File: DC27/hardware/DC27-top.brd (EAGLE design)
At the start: 102.4 x 117.6 mm, 32 parts

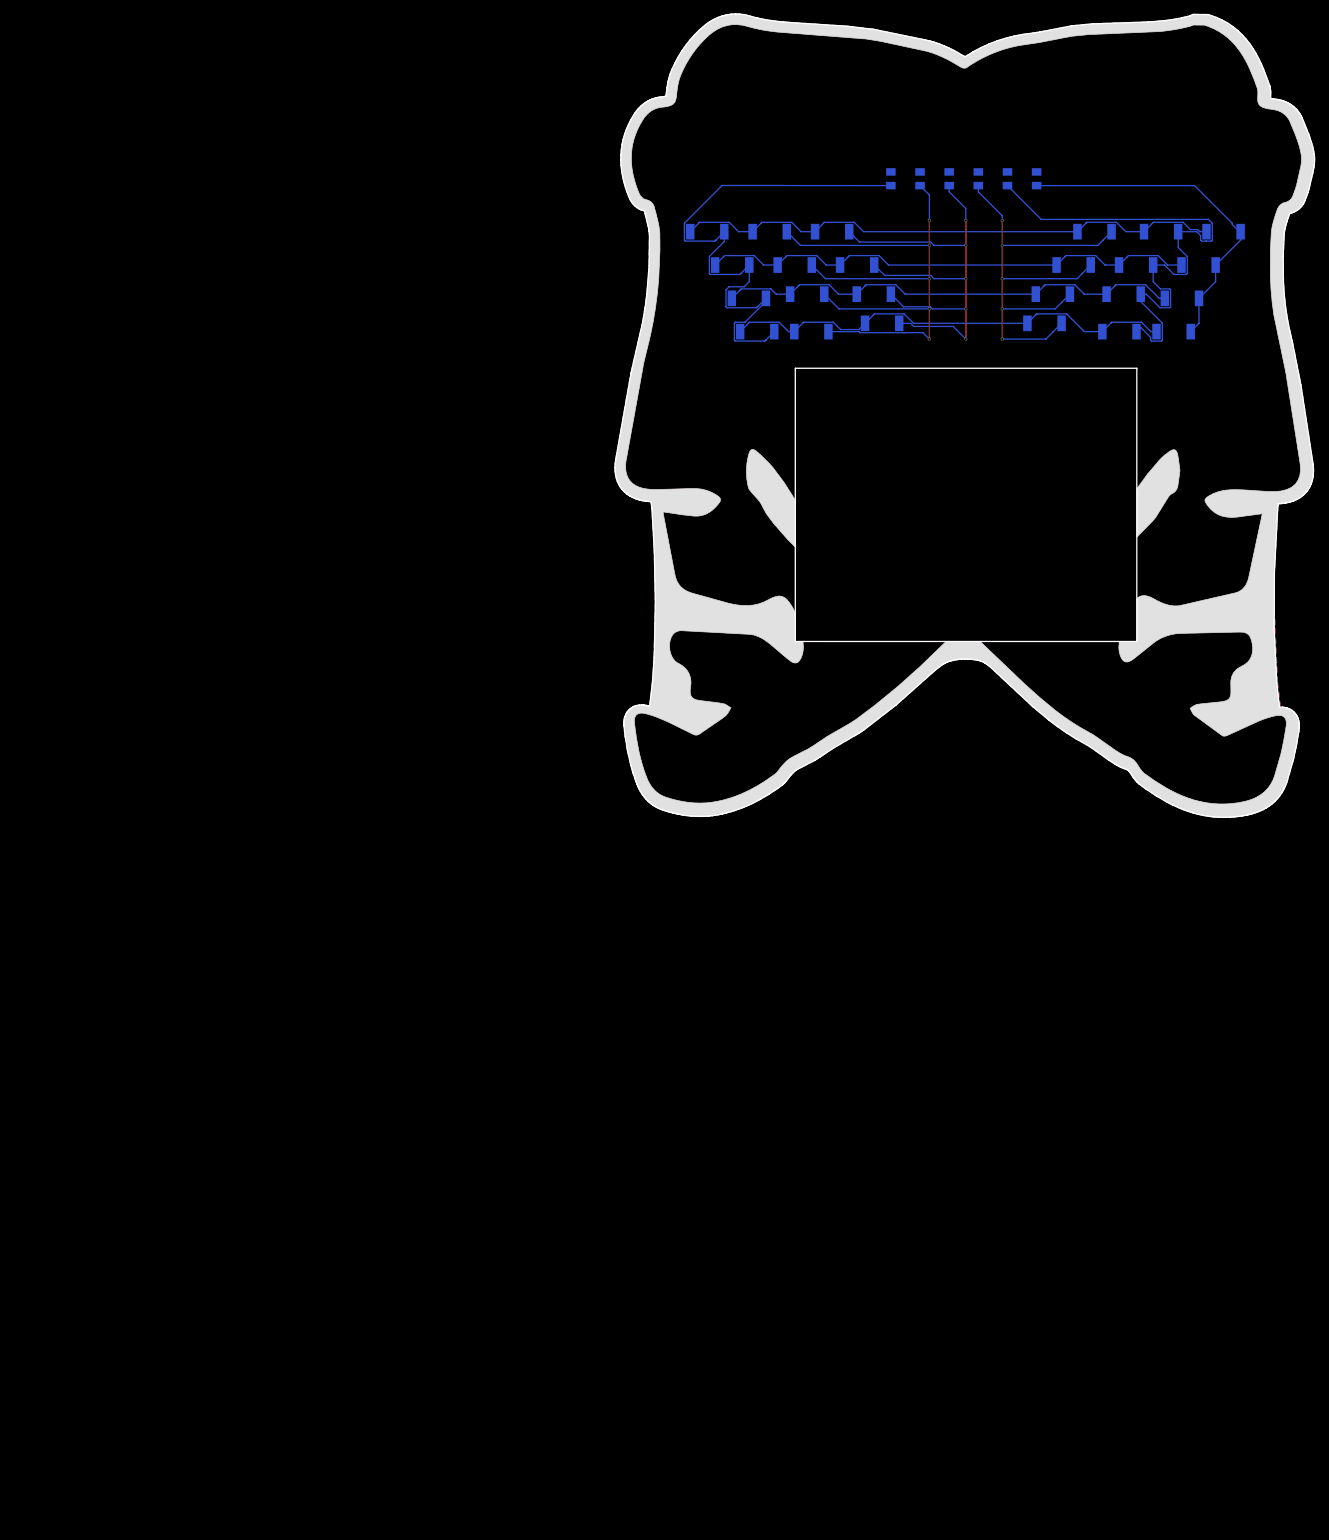
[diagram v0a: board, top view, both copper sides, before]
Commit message: adding basic layout dc27 badge
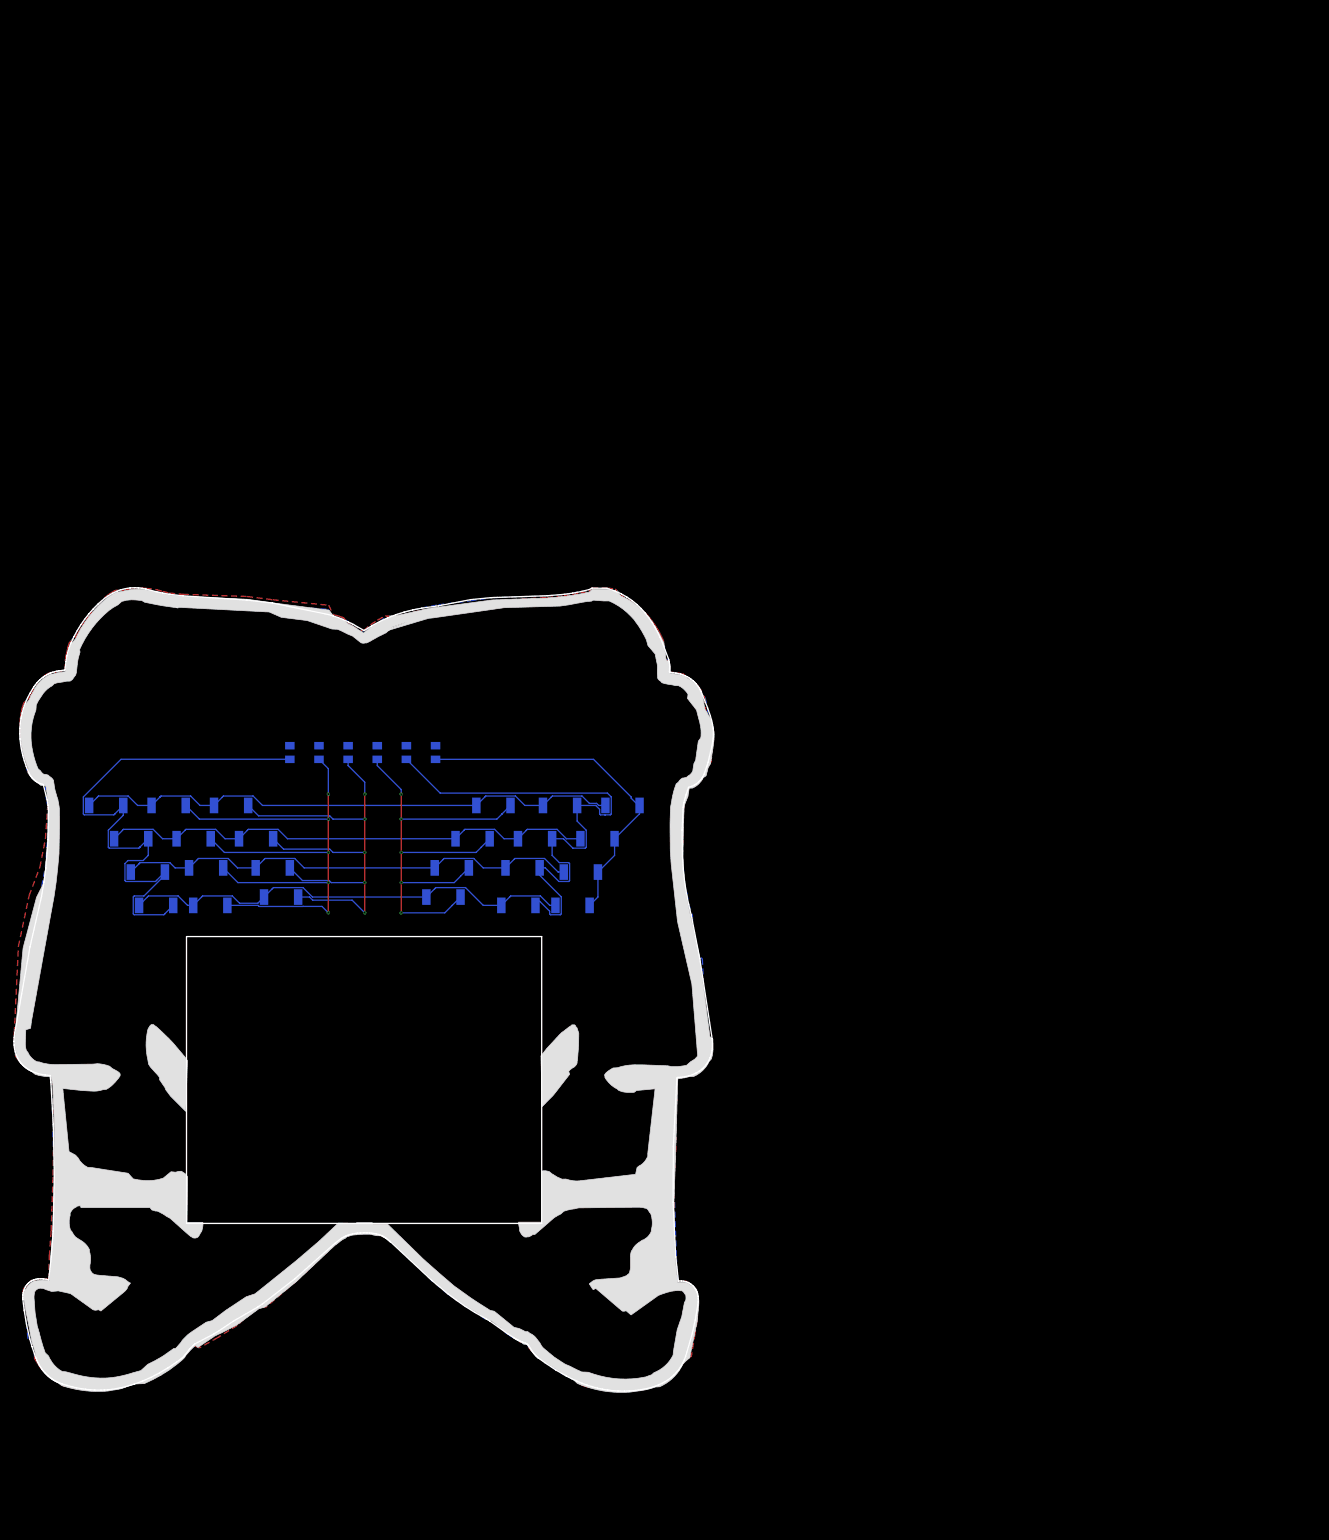
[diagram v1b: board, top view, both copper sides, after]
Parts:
- moved LED12 121.7 mm to (38.2, 82.4)
- moved LED13 121.7 mm to (40.6, 78.2)
- moved LED14 121.7 mm to (41.8, 73.9)
- moved LED17 121.7 mm to (69.9, 82.4)
- moved LED18 121.7 mm to (66.8, 78.2)
- moved LED19 121.7 mm to (65.6, 73.9)
- moved LED2 121.7 mm to (19.9, 82.4)
- moved LED23 121.7 mm to (77.2, 78.2)
- moved LED24 121.7 mm to (76.6, 72.7)
- moved LED3 121.7 mm to (22.3, 77.5)
- moved LED4 121.7 mm to (23.6, 72.7)
- moved LED7 121.7 mm to (29.0, 82.4)
- moved LED8 121.7 mm to (30.9, 78.2)
- moved LED9 121.7 mm to (31.5, 72.7)
- moved LED16 121.7 mm to (72.9, 87.3)
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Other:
- outline, holes or cut-outs redrawn

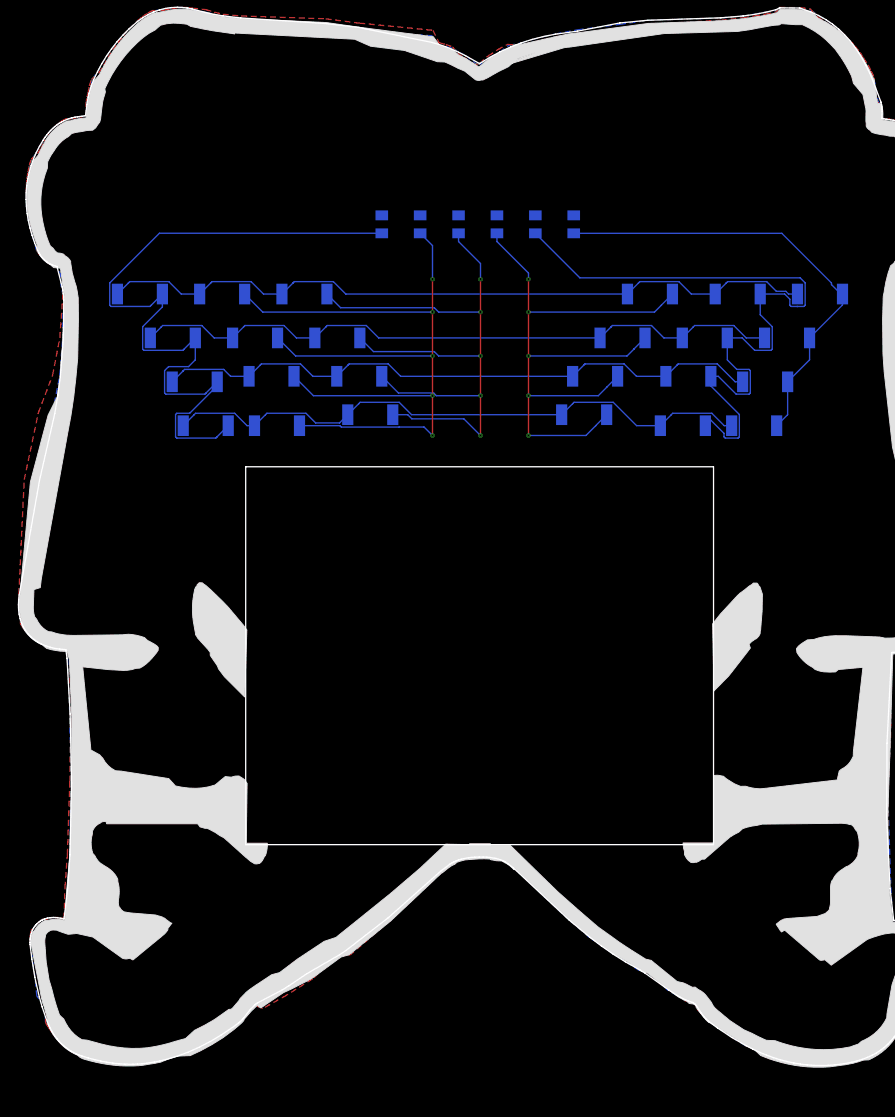
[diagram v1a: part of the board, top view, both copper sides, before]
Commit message: started on changes to not charlie plex the leds
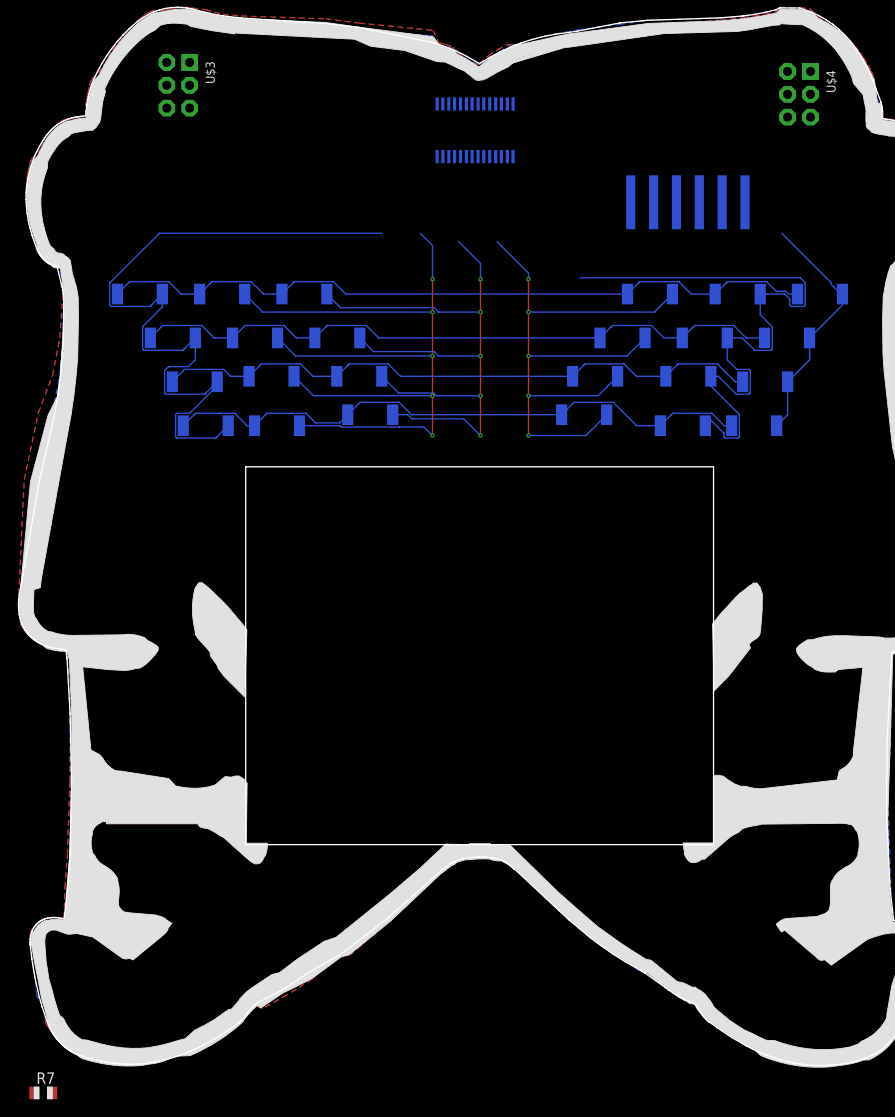
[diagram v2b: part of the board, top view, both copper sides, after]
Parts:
- removed R1, R2, R3, R4, R5, R6: (no value), darknet_parts_library:R0805
- added J1: POGO_CONNECTOR, connector:1X06_SMD_MALE
- added R7: 1 K, darknet_parts_library:R0805
- added U$3, U$4: DC-27-SAO, defcon:3X2
- added U1: TLC59116IPWR, leds:SOP65P640X120-28N
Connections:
- new net GND: J1.6, R7.2, U$3.4, U$4.4, U1.10, U1.19, U1.2, U1.24, U1.3, U1.4, U1.5
- new net GPIO1: J1.4, U$3.3, U$4.3
- new net GPIO2: J1.5, U$3.6, U$4.6
- new net N$10: U1.13
- new net N$18: R7.1, U1.1
- new net N$19: U1.14
- new net N$20: U1.25
- new net N$21: U1.15
- new net N$22: U1.16
- new net SCL: J1.2, U$3.5, U$4.5, U1.26
- new net SDA: J1.3, U$3.2, U$4.2, U1.27
- new net VCC: J1.1, U$3.1, U$4.1, U1.28
- net N$11: no longer R6.1
- net N$12: now also U1.12; no longer R1.2
- net N$13: now also U1.11; no longer R2.2
- net N$14: now also U1.9; no longer R3.2
- net N$15: now also U1.8; no longer R4.2
- net N$16: now also U1.7; no longer R5.2
- net N$17: now also U1.6; no longer R6.2
- net N$5: no longer R1.1
- net N$6: no longer R2.1
- net N$7: no longer R3.1
- net N$8: no longer R4.1
- net N$9: no longer R5.1
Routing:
- net N$11: track 50.5 -> 27.4 mm
- net N$9: track 79.5 -> 72.5 mm
- net N$8: track 75.0 -> 74.1 mm
- net N$7: track 78.2 -> 77.3 mm

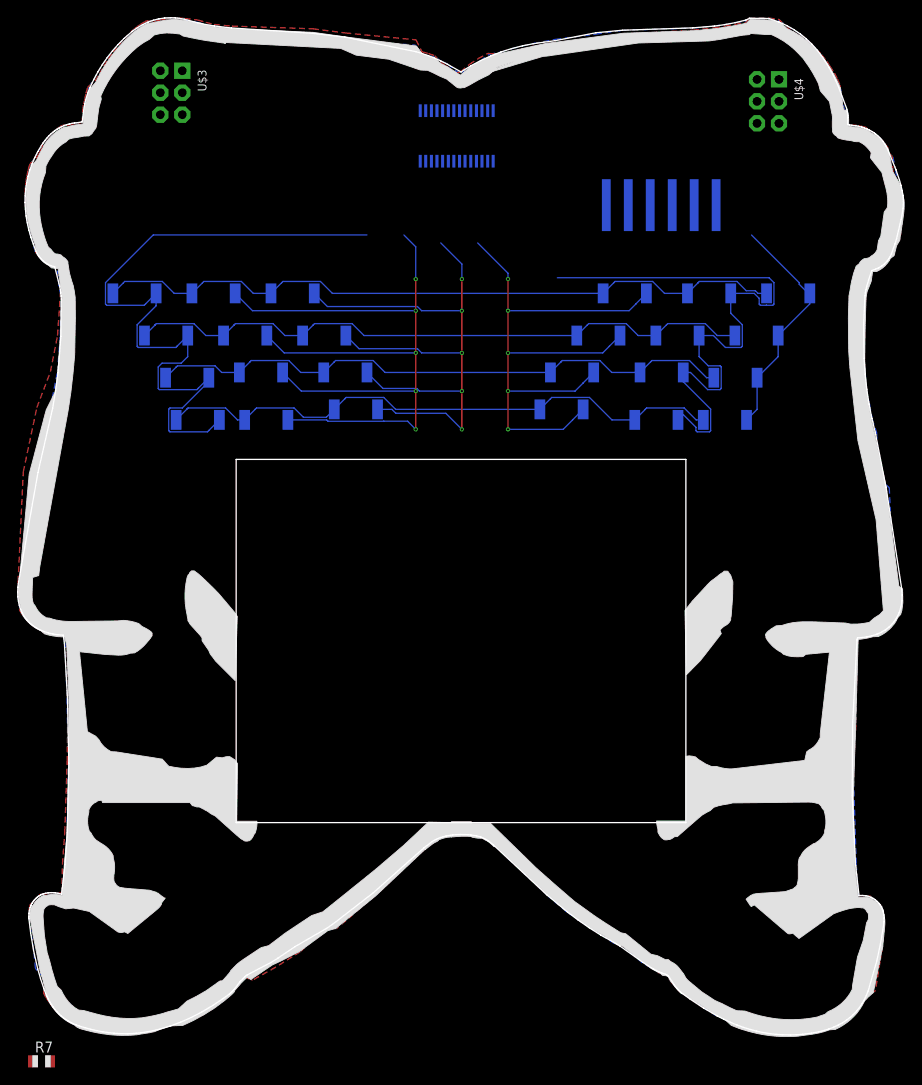
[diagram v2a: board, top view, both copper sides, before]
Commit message: top board farther, made a breakout board for new led driver
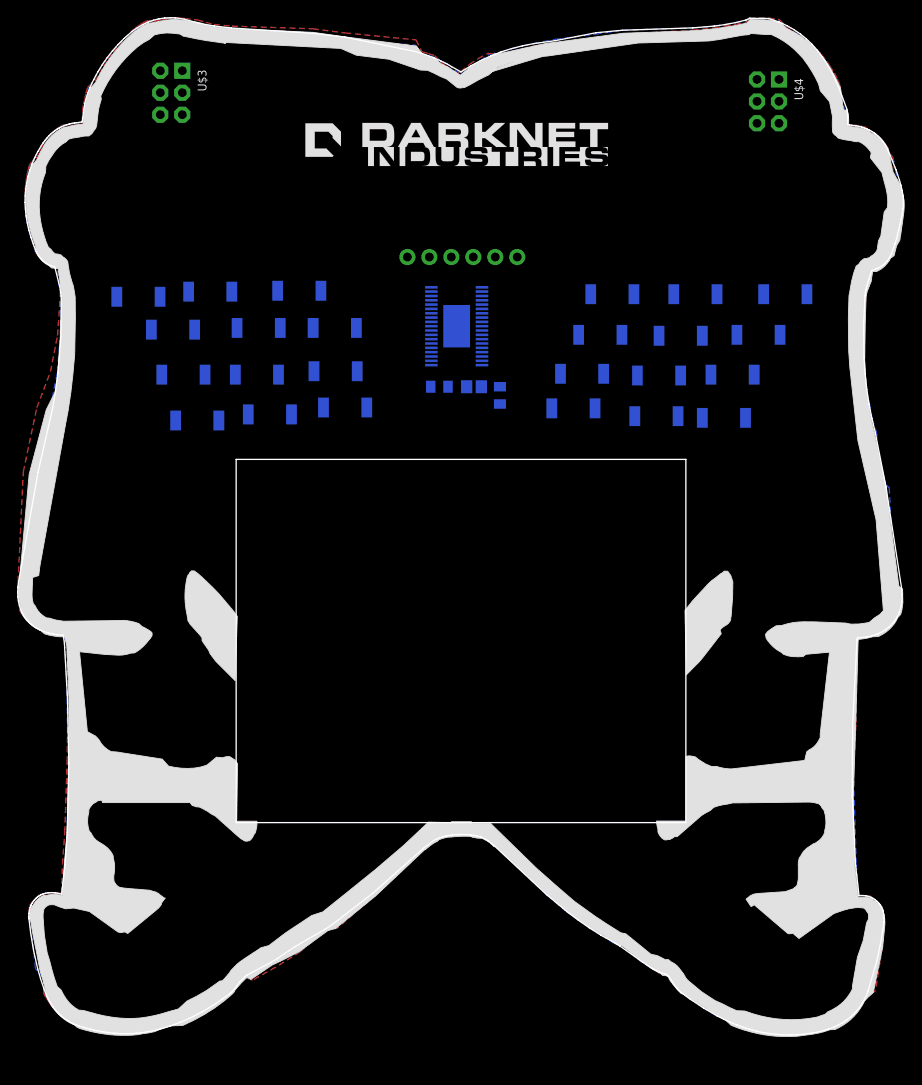
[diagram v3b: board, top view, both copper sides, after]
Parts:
- removed LED26, LED27, LED28, LED29: (no value), darknet_parts_library:GULLWING_LED
- removed U1: TLC59116IPWR, leds:SOP65P640X120-28N
- added C1: 0.1 uF, passives:C0805
- added IC1: PCA9956BTWY, PCA9956BTWY:SOP50P640X110-39N
- added LED10, LED15, LED20, LED5: (no value), leds:GULLWING_LED
- added R2: 10 K, darknet_parts_library:R0805
- added U$5: DN_LOGODC26, logos:DN_LOGO_DC26
- J1: value POGO_CONNECTOR -> top-bot-connector; device connector:1X06_SMD_MALE -> connector:1X06
- LED1, LED11, LED12, LED13, LED14, LED16, LED17, LED18, LED19, LED2, LED21, LED22, LED23, LED24, LED3, LED4, LED6, LED7, LED8, LED9: device darknet_parts_library:GULLWING_LED -> leds:GULLWING_LED
- R7: value 1 K -> 2 K
- U$2: device darknet_parts_library:CMD_C0DE_LOGO -> logos:CMD_C0DE_LOGO
- moved U$2 92.9 mm to (91.0, 8.00)
- moved U$1 91.0 mm to (9.49, 9.16)
- moved R7 90.6 mm to (49.0, 75.0), flipped to the bottom, turned to 180 degrees
- moved LED13 51.7 mm to (91.5, 87.2)
- moved LED14 41.5 mm to (81.1, 87.2)
- moved LED12 26.5 mm to (11.7, 83.9), turned to 180 degrees
- moved LED1 25.2 mm to (35.6, 71.1), turned to 180 degrees
- moved J1 23.8 mm to (58.0, 90.0)
- moved LED19 20.2 mm to (85.4, 77.9)
- moved LED21 17.4 mm to (68.0, 78.0)
- moved LED16 16.2 mm to (88.4, 82.5)
- moved LED8 15.3 mm to (15.7, 80.1), turned to 180 degrees
- moved LED6 15.0 mm to (16.9, 74.9), turned to 180 degrees
- moved LED11 14.8 mm to (20.0, 84.5), turned to 180 degrees
- moved LED2 14.0 mm to (26.9, 70.3), turned to 180 degrees
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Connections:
- new net N$23: IC1.32, LED23.A
- new net N$24: IC1.33, LED24.A
- new net N$35: IC1.1, R7.1
- new net N$36: IC1.35, R2.2
- net GND: now also C1.1, IC1.14, IC1.18, IC1.2, IC1.21, IC1.25, IC1.3, IC1.34, IC1.39, IC1.5, LED1.C, LED10.C, LED11.C, LED12.C, LED13.C, LED14.C, LED15.C, LED16.C, LED17.C, LED18.C, LED19.C, LED2.C, LED20.C, LED21.C, LED22.C, LED23.C, LED24.C, LED3.C, LED4.C, LED5.C, LED6.C, LED7.C, LED8.C, LED9.C; no longer U1.10, U1.19, U1.2, U1.24, U1.3, U1.4, U1.5
- net N$1: now also IC1.6; no longer LED11.A, LED16.A, LED21.A, LED26.A, LED6.A
- net N$10: now also IC1.16, LED10.A; no longer U1.13
- net N$11: now also IC1.17, LED11.A; no longer LED26.C, LED27.C, LED28.C, LED29.C
- net N$12: now also IC1.19, LED12.A; no longer U1.12
- net N$13: now also IC1.20, LED13.A; no longer U1.11
- net N$14: now also IC1.22, LED14.A; no longer U1.9
- net N$15: now also IC1.23, LED15.A; no longer U1.8
- net N$16: now also IC1.24, LED16.A; no longer U1.7
- net N$17: now also IC1.26, LED17.A; no longer U1.6
- net N$18: now also IC1.27, LED18.A; no longer R7.1, U1.1
- net N$19: now also IC1.28, LED19.A; no longer U1.14
- net N$2: now also IC1.7; no longer LED12.A, LED17.A, LED22.A, LED27.A, LED7.A
- net N$20: now also IC1.29, LED20.A; no longer U1.25
- net N$21: now also IC1.30, LED21.A; no longer U1.15
- net N$22: now also IC1.31, LED22.A; no longer U1.16
- net N$3: now also IC1.8; no longer LED13.A, LED18.A, LED23.A, LED28.A, LED8.A
- net N$4: now also IC1.9; no longer LED14.A, LED19.A, LED24.A, LED29.A, LED9.A
- net N$5: now also IC1.10, LED5.A; no longer LED1.C, LED2.C, LED3.C, LED4.C
- net N$6: now also IC1.11, LED6.A; no longer LED6.C, LED7.C, LED8.C, LED9.C
- net N$7: now also IC1.12, LED7.A; no longer LED11.C, LED12.C, LED13.C, LED14.C
- net N$8: now also IC1.13, LED8.A; no longer LED16.C, LED17.C, LED18.C, LED19.C
- net N$9: now also IC1.15, LED9.A; no longer LED21.C, LED22.C, LED23.C, LED24.C
- net SCL: now also IC1.36; no longer U1.26
- net SDA: now also IC1.37; no longer U1.27
- net VCC: now also C1.2, IC1.38, R2.1; no longer U1.28
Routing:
- net N$6: track 94.3 -> 0.00 mm, vias 5 -> 0
- net N$5: track 85.7 -> 0.00 mm
- net N$1: track 81.3 -> 0.00 mm
- net N$7: track 77.3 -> 0.00 mm, vias 5 -> 0
- net N$8: track 74.1 -> 0.00 mm, vias 5 -> 0
- net N$2: track 74.0 -> 0.00 mm
- net N$9: track 72.5 -> 0.00 mm
- net N$3: track 69.1 -> 0.00 mm
- net N$4: track 67.5 -> 0.00 mm
- net N$11: track 27.4 -> 0.00 mm
